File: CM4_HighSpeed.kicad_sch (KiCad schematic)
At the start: 4 parts, among them J7 Conn_01x22

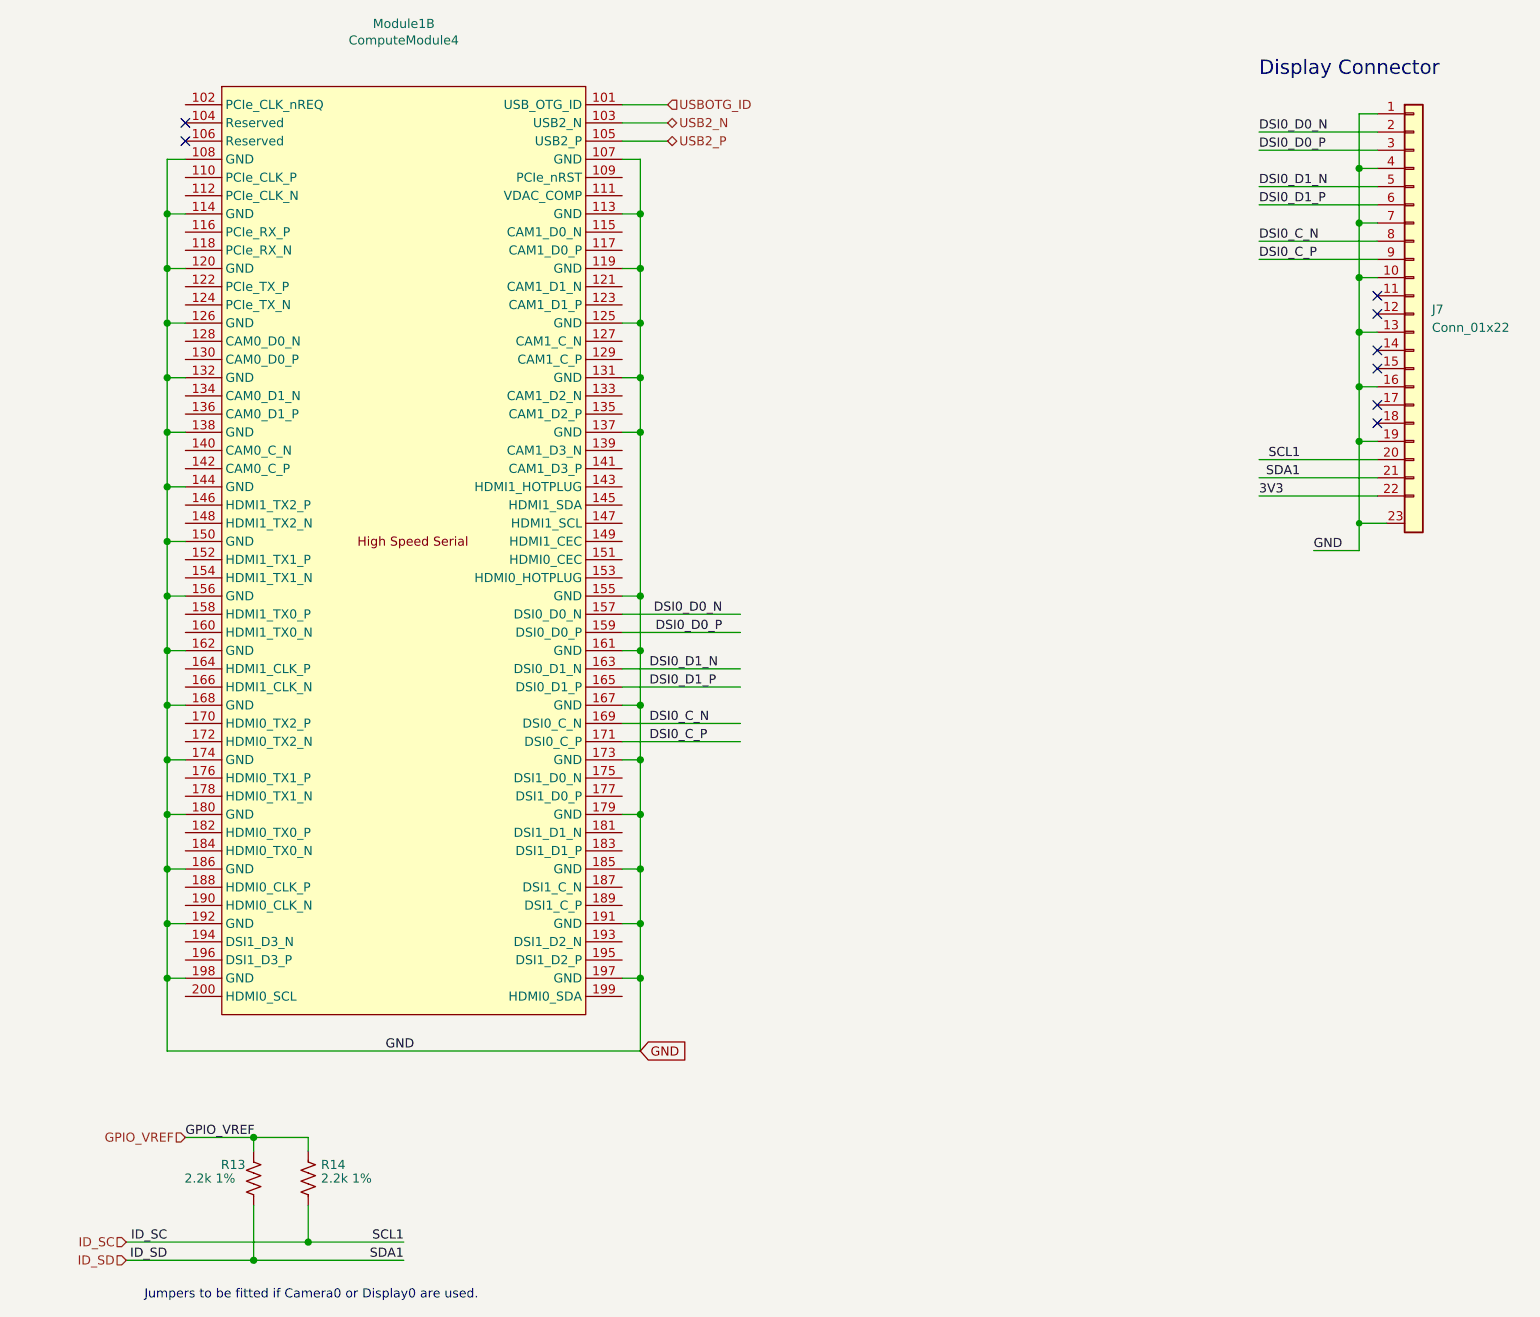
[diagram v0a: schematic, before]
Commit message: added more USB ports.. placing
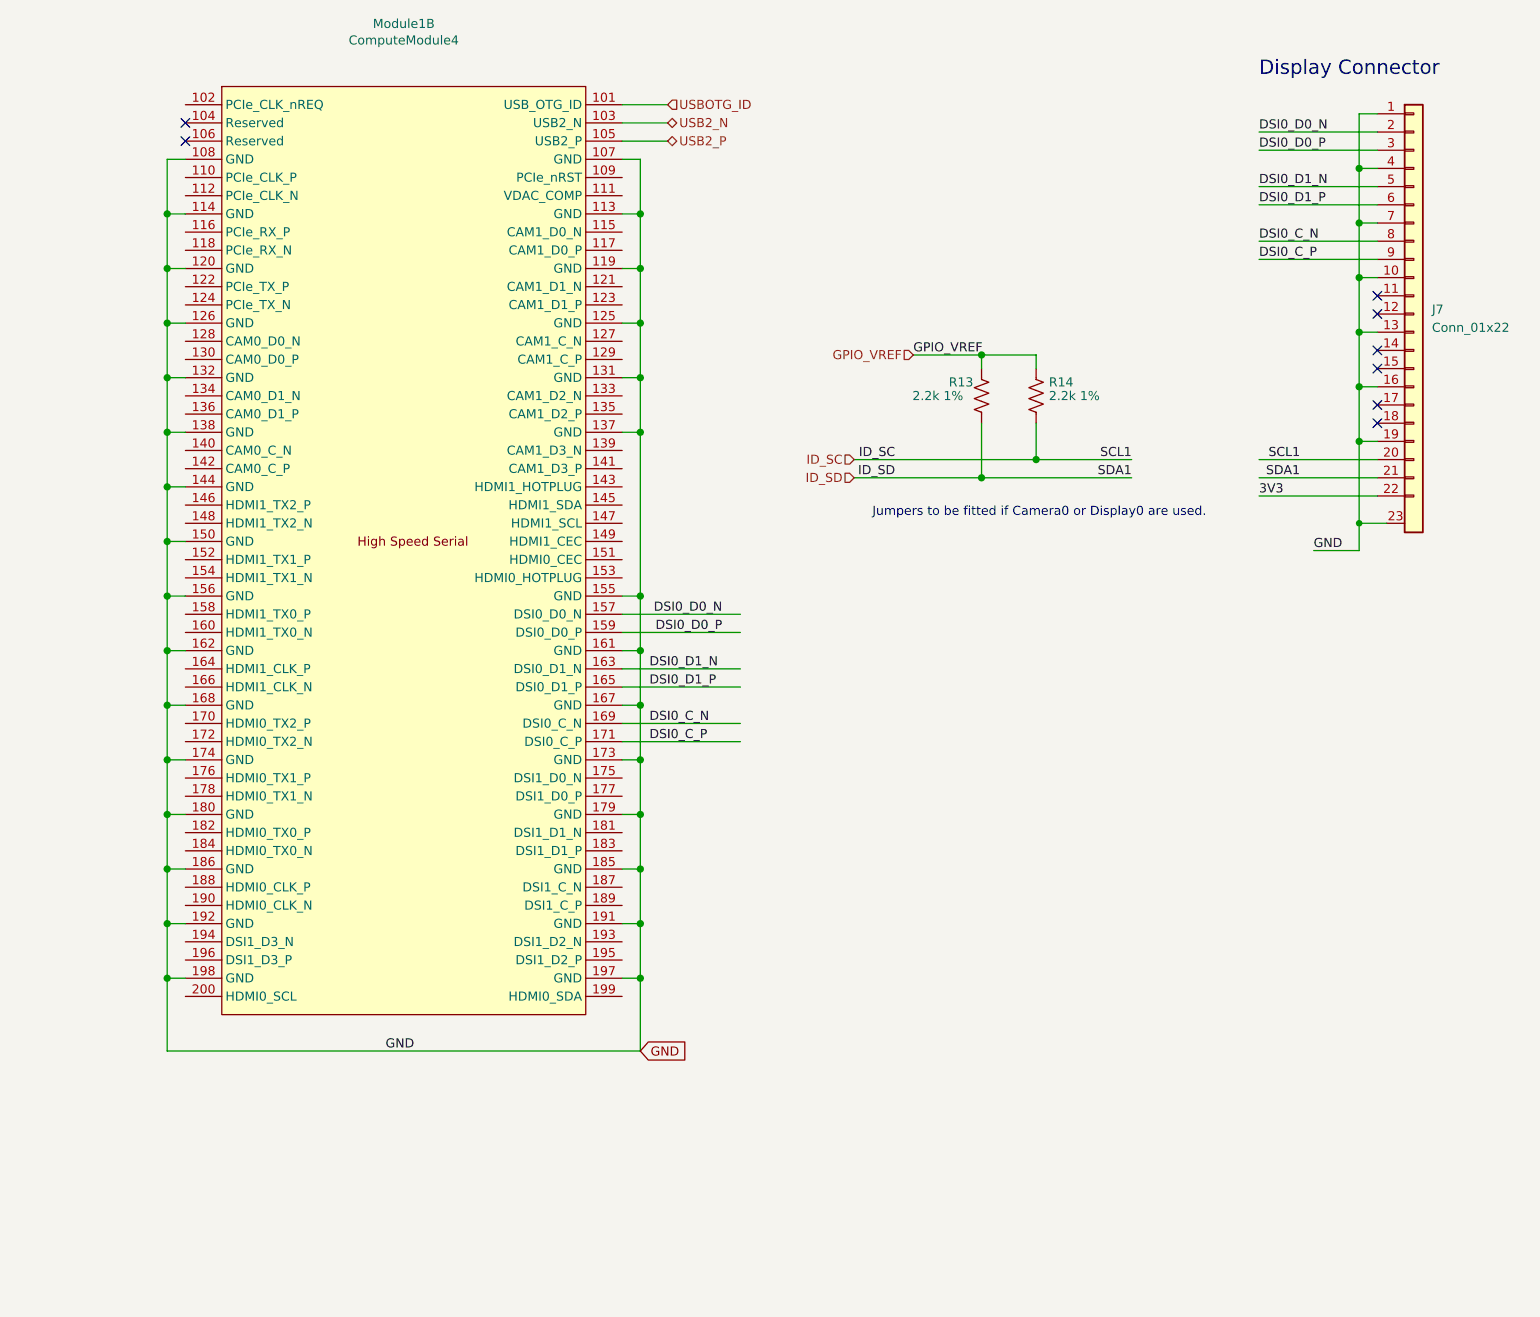
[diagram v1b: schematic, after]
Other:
- moved on the sheet: R13, R14
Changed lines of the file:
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@@
 	)
 	(junction
-		(at 51.435 187.96)
+		(at 153.035 78.74)
 		(diameter 1.016)
 		(color 0 0 0 0)
@@
 	)
 	(junction
-		(at 51.435 170.815)
+		(at 153.035 61.595)
 		(diameter 1.016)
 		(color 0 0 0 0)
@@
 	)
 	(junction
-		(at 59.055 185.42)
+		(at 160.655 76.2)
 		(diameter 1.016)
 		(color 0 0 0 0)
@@
 	(wire
 		(pts
-			(xy 33.655 185.42) (xy 59.055 185.42)
+			(xy 135.255 76.2) (xy 160.655 76.2)
 		)
 		(stroke
@@
 	(wire
 		(pts
-			(xy 59.055 180.34) (xy 59.055 185.42)
+			(xy 160.655 71.12) (xy 160.655 76.2)
 		)
 		(stroke
@@
 	(wire
 		(pts
-			(xy 51.435 170.815) (xy 59.055 170.815)
+			(xy 153.035 61.595) (xy 160.655 61.595)
 		)
 		(stroke
@@
 	(wire
 		(pts
-			(xy 51.435 187.96) (xy 72.39 187.96)
-		)
-		(stroke
-			(width 0)
-			(type solid)
-		)
-	)
-	(wire
-		(pts
-			(xy 51.435 170.815) (xy 51.435 172.72)
+			(xy 153.035 78.74) (xy 173.99 78.74)
+		)
+		(stroke
+			(width 0)
+			(type solid)
+		)
+	)
+	(wire
+		(pts
+			(xy 153.035 61.595) (xy 153.035 63.5)
 		)
 		(stroke
@@
 	(wire
 		(pts
-			(xy 59.055 170.815) (xy 59.055 172.72)
+			(xy 160.655 61.595) (xy 160.655 63.5)
 		)
 		(stroke
@@
 	(wire
 		(pts
-			(xy 51.435 180.34) (xy 51.435 187.96)
+			(xy 153.035 71.12) (xy 153.035 78.74)
 		)
 		(stroke
@@
 	(wire
 		(pts
-			(xy 41.91 170.815) (xy 51.435 170.815)
+			(xy 143.51 61.595) (xy 153.035 61.595)
 		)
 		(stroke
@@
 	(wire
 		(pts
-			(xy 33.655 187.96) (xy 51.435 187.96)
-		)
-		(stroke
-			(width 0)
-			(type solid)
-		)
-	)
-	(wire
-		(pts
-			(xy 59.055 185.42) (xy 72.39 185.42)
+			(xy 135.255 78.74) (xy 153.035 78.74)
+		)
+		(stroke
+			(width 0)
+			(type solid)
+		)
+	)
+	(wire
+		(pts
+			(xy 160.655 76.2) (xy 173.99 76.2)
 		)
 		(stroke
@@
 	(text "Jumpers to be fitted if Camera0 or Display0 are used.\n"
 		(exclude_from_sim no)
-		(at 82.804 193.548 0)
+		(at 184.404 84.328 0)
 		(effects
 			(font
@@
 	)
 	(label "SCL1"
-		(at 72.39 185.42 180)
+		(at 173.99 76.2 180)
 		(fields_autoplaced yes)
 		(effects
@@
 	)
 	(label "GPIO_VREF"
-		(at 41.91 170.815 0)
+		(at 143.51 61.595 0)
 		(fields_autoplaced yes)
 		(effects
@@
 	)
 	(label "SDA1"
-		(at 72.39 187.96 180)
+		(at 173.99 78.74 180)
 		(fields_autoplaced yes)
 		(effects
@@
 	)
 	(label "ID_SC"
-		(at 39.37 185.42 180)
+		(at 140.97 76.2 180)
 		(fields_autoplaced yes)
 		(effects
@@
 	)
 	(label "ID_SD"
-		(at 39.37 187.96 180)
+		(at 140.97 78.74 180)
 		(fields_autoplaced yes)
 		(effects
@@
 	(hierarchical_label "ID_SC"
 		(shape input)
-		(at 33.655 185.42 180)
+		(at 135.255 76.2 180)
 		(fields_autoplaced yes)
 		(effects
@@
 	(hierarchical_label "ID_SD"
 		(shape input)
-		(at 33.655 187.96 180)
+		(at 135.255 78.74 180)
 		(fields_autoplaced yes)
 		(effects
@@
 	(hierarchical_label "GPIO_VREF"
 		(shape input)
-		(at 41.91 170.815 180)
+		(at 143.51 61.595 180)
 		(fields_autoplaced yes)
 		(effects
@@
 	(symbol
 		(lib_id "Device:R_US")
-		(at 51.435 176.53 0)
+		(at 153.035 67.31 0)
 		(unit 1)
 		(exclude_from_sim no)
@@
 		(dnp no)
 		(property "Reference" "R13"
-			(at 46.863 174.625 0)
+			(at 148.463 65.405 0)
 			(effects
 				(font
@@
 		)
 		(property "Value" "2.2k 1%"
-			(at 41.783 176.53 0)
+			(at 143.383 67.31 0)
 			(effects
 				(font
@@
 		)
 		(property "Footprint" "Resistor_SMD:R_0402_1005Metric"
-			(at 49.657 176.53 90)
+			(at 151.257 67.31 90)
 			(effects
 				(font
@@
 		)
 		(property "Datasheet" "https://fscdn.rohm.com/en/products/databook/datasheet/passive/resistor/chip_resistor/mcr-e.pdf"
-			(at 51.435 176.53 0)
+			(at 153.035 67.31 0)
 			(effects
 				(font
@@
 		)
 		(property "Description" ""
-			(at 51.435 176.53 0)
+			(at 153.035 67.31 0)
 			(effects
 				(font
@@
 		)
 		(property "DK" "311-2.20KLRCT-ND"
-			(at 51.435 176.53 0)
+			(at 153.035 67.31 0)
 			(effects
 				(font
@@
 		)
 		(property "PARTNO" "RC0402FR-072K2L"
-			(at 51.435 176.53 0)
+			(at 153.035 67.31 0)
 			(effects
 				(font
@@
 	(symbol
 		(lib_id "Device:R_US")
-		(at 59.055 176.53 0)
+		(at 160.655 67.31 0)
 		(unit 1)
 		(exclude_from_sim no)
@@
 		(dnp no)
 		(property "Reference" "R14"
-			(at 60.833 174.625 0)
+			(at 162.433 65.405 0)
 			(effects
 				(font
@@
 		)
 		(property "Value" "2.2k 1%"
-			(at 60.833 176.53 0)
+			(at 162.433 67.31 0)
 			(effects
 				(font
@@
 		)
 		(property "Footprint" "Resistor_SMD:R_0402_1005Metric"
-			(at 57.277 176.53 90)
+			(at 158.877 67.31 90)
 			(effects
 				(font
@@
 		)
 		(property "Datasheet" "https://fscdn.rohm.com/en/products/databook/datasheet/passive/resistor/chip_resistor/mcr-e.pdf"
-			(at 59.055 176.53 0)
+			(at 160.655 67.31 0)
 			(effects
 				(font
@@
 		)
 		(property "Description" ""
-			(at 59.055 176.53 0)
+			(at 160.655 67.31 0)
 			(effects
 				(font
@@
 		)
 		(property "PARTNO" "RC0402FR-072K2L"
-			(at 59.055 176.53 0)
+			(at 160.655 67.31 0)
 			(effects
 				(font
@@
 		)
 		(property "DK" "311-2.20KLRCT-ND"
-			(at 59.055 176.53 0)
+			(at 160.655 67.31 0)
 			(effects
 				(font
